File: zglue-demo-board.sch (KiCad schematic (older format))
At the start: 146 parts, among them J1 3220-10-0100-00, J10 0473460001, J2 DF13A-2P-1.25H, J3 3220-10-0100-00, J4 2x20_Header_Female, J5 0473460001, J6 556500488, J7 556500488, J8 WE_686115148922, J9 WE_686115148922_FLIPPED, U1 MCP1700T-3302E_TT, U2 NTS0104BQ, U3 NTS0104BQ, U4 NTS0104BQ, U5 93LC56CT-IMC, U6 FT4232HQ, U7 NTB0104BQ, U8 NTB0104BQ, Y1 ASFLMB-12.000MHZ-LC-T

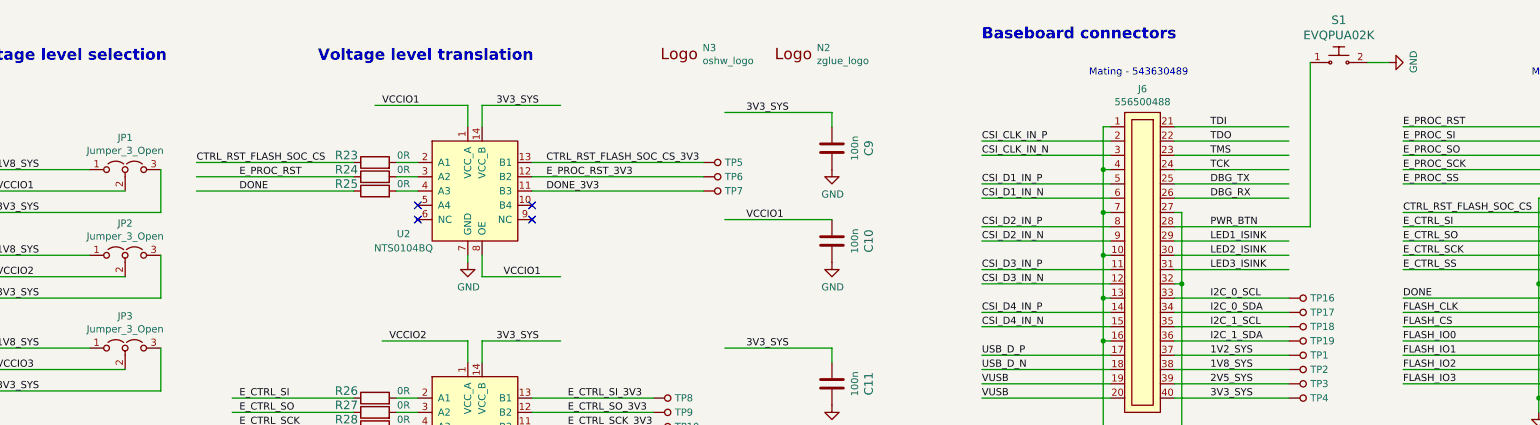
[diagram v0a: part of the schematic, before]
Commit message: Connected PWR_BTN to VUSB, updated PCB
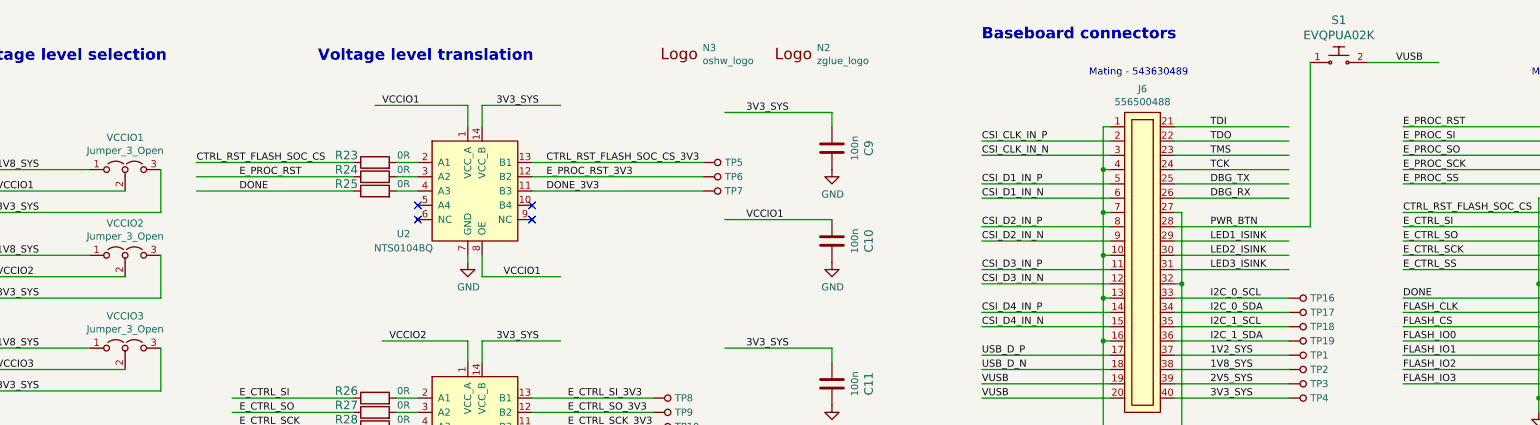
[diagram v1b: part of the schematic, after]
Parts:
- renumbered JP1 to VCCIO1, JP2 to VCCIO2, JP3 to VCCIO3
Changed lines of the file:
@@
 $EndComp
 $Comp
-L zglue-demo-board-rescue:Jumper_3_Open-Jumper JP2
+L zglue-demo-board-rescue:Jumper_3_Open-Jumper VCCIO2
 U 1 1 5F6F7935
 P 4350 2200
-F 0 "JP2" H 4350 2424 50  0000 C CNN
+F 0 "VCCIO2" H 4350 2424 50  0000 C CNN
 F 1 "Jumper_3_Open" H 4350 2333 50  0000 C CNN
 F 2 "Jumper:SolderJumper-3_P1.3mm_Open_Pad1.0x1.5mm" H 4350 2200 50  0001 C CNN
@@
 	4600 2500 3350 2500
 $Comp
-L zglue-demo-board-rescue:Jumper_3_Open-Jumper JP3
+L zglue-demo-board-rescue:Jumper_3_Open-Jumper VCCIO3
 U 1 1 5FF28200
 P 4350 2850
-F 0 "JP3" H 4350 3074 50  0000 C CNN
+F 0 "VCCIO3" H 4350 3074 50  0000 C CNN
 F 1 "Jumper_3_Open" H 4350 2983 50  0000 C CNN
 F 2 "Jumper:SolderJumper-3_P1.3mm_Open_Pad1.0x1.5mm" H 4350 2850 50  0001 C CNN
@@
 	4600 3150 3350 3150
 $Comp
-L zglue-demo-board-rescue:Jumper_3_Open-Jumper JP1
+L zglue-demo-board-rescue:Jumper_3_Open-Jumper VCCIO1
 U 1 1 5FF6DF38
 P 4350 1600
-F 0 "JP1" H 4350 1824 50  0000 C CNN
+F 0 "VCCIO1" H 4350 1824 50  0000 C CNN
 F 1 "Jumper_3_Open" H 4350 1733 50  0000 C CNN
 F 2 "Jumper:SolderJumper-3_P1.3mm_Open_Pad1.0x1.5mm" H 4350 1600 50  0001 C CNN
@@
 Wire Wire Line
 	11700 2000 12650 2000
-$Comp
-L power:GND #PWR0103
-U 1 1 5DCDFECB
-P 13200 850
-F 0 "#PWR0103" H 13200 600 50  0001 C CNN
-F 1 "GND" H 13205 677 50  0000 C CNN
-F 2 "" H 13200 850 50  0001 C CNN
-F 3 "" H 13200 850 50  0001 C CNN
-	1    13200 850
-	0    -1   -1   0
-$EndComp
-Wire Wire Line
-	13200 850  13050 850
+Wire Wire Line
+	13550 850  13050 850
 $Comp
 L antmicroLEDIndicationDiscrete:LG_L29K-G2J1-24-Z D9
@@
 	1    0    0    -1
 $EndComp
+Text Label 13250 850  0    50   ~ 0
+VUSB
 $EndSCHEMATC

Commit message: Layout components moved away from PCB edges
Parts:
- C1, C2, C3, C4, C5: footprint antmicro-footprints:0603-cap -> zglue-demo-board-footprints:0603-cap; symbol antmicroCapacitors0603:C_1u_0603 -> zglue-demo-board:C_1u_0603
- C10, C11, C12, C13, C14, C15, C16, C17, C18, C19, C20, C21, C22, C23, C24, C9: footprint antmicro-footprints:0402-cap -> zglue-demo-board-footprints:0402-cap; symbol antmicroCapacitors0402:C_100n_0402_6V3 -> zglue-demo-board:C_100n_0402_6V3
- C25, C26: footprint antmicro-footprints:0402-cap -> zglue-demo-board-footprints:0402-cap; symbol antmicroCapacitors0402:C_4u7_0402 -> zglue-demo-board:C_4u7_0402
- D1, D3, D4: footprint antmicro-footprints:SOD-123 -> zglue-demo-board-footprints:SOD-123; symbol antmicroDiodesRectifiersSingle:MBR0540T1G -> zglue-demo-board:MBR0540T1G
- D10, D11, D12, D13, D6, D7, D8, D9: footprint antmicro-footprints:LED_0603 -> zglue-demo-board-footprints:LED_0603; symbol antmicroLEDIndicationDiscrete:LG_L29K-G2J1-24-Z -> zglue-demo-board:LG_L29K-G2J1-24-Z
- D2, D5: footprint antmicro-footprints:SOT-3 -> zglue-demo-board-footprints:SOT-3; symbol antmicroTVSDiodes:TPD2EUSB30DRTR -> zglue-demo-board:TPD2EUSB30DRTR
- FB1, FB2: footprint antmicro-footprints:0603-res -> zglue-demo-board-footprints:0603; symbol antmicroFerriteBeadsandChips:BLM18AG601SN1D -> zglue-demo-board:BLM18AG601SN1D
- J1, J3: footprint antmicro-footprints:PinHeader_2x5_P1.27mm_Drill.7mm -> zglue-demo-board-footprints:PinHeader_2x5_P1.27mm_Drill.7mm; symbol antmicroRectangularConnectorsHeadersMalePins:3220-10-0100-00 -> zglue-demo-board:3220-10-0100-00
- J10, J5: footprint antmicro-footprints:USB_Micro_B_Female_0473460001 -> zglue-demo-board-footprints:USB_Micro_B_Female_0473460001; symbol antmicroUSBDVIHDMIConnectors:0473460001 -> zglue-demo-board:0473460001
- J2: footprint antmicro-footprints:DF13A-2P-1.25H -> zglue-demo-board-footprints:DF13A-2P-1.25H; symbol antmicroDF13Connectors:DF13A-2P-1.25H -> zglue-demo-board:DF13A-2P-1.25H
- J4: footprint antmicro-footprints:PinHeader_2x40_P2.54_Drill1mm -> zglue-demo-board-footprints:PinHeader_2x40_P2.54_Drill1mm; symbol antmicroRectangularConnectorsHeadersFemalePins:2x20_Header_Female -> zglue-demo-board:2x20_Header_Female
- J6, J7: footprint antmicro-footprints:556500488 -> zglue-demo-board-footprints:556500488; symbol antmicroB2bConnectors:556500488 -> zglue-demo-board:556500488; MPN (none) -> 556500488; Manufacturer (none) -> Molex
- J8: footprint antmicro-footprints:WE_686115148922 -> zglue-demo-board-footprints:WE_686115148922; symbol antmicroFCCConnectors:WE_686115148922 -> zglue-demo-board:WE_686115148922
- J9: footprint antmicro-footprints:WE_686115148922_FLIPPED -> zglue-demo-board-footprints:WE_686115148922_FLIPPED; symbol antmicroFCCConnectors:WE_686115148922_FLIPPED -> zglue-demo-board:WE_686115148922_FLIPPED
- N1: footprint antmicro-footprints:antmicro-logo_scaled_20mm -> zglue-demo-board-footprints:antmicro-logo; symbol antmicroMechanicalParts:antmicro_logo -> zglue-demo-board:antmicro_logo
- N2: footprint antmicro-footprints:zglue-logo -> zglue-demo-board-footprints:zglue-logo; symbol antmicroMechanicalParts:zglue_logo -> zglue-demo-board:zglue_logo
- N3: footprint antmicro-footprints:oshw-logo -> zglue-demo-board-footprints:oshw-logo; symbol antmicroMechanicalParts:oshw_logo -> zglue-demo-board:oshw_logo
- R1: footprint antmicro-footprints:0603-res -> zglue-demo-board-footprints:0603-res; symbol antmicroResistors0603:R_0R_0603 -> zglue-demo-board:R_0R_0603
- R10, R5: footprint antmicro-footprints:0402-res -> zglue-demo-board-footprints:0402-res; symbol antmicroResistors0402:R_2k_0402 -> zglue-demo-board:R_2k_0402
- R11, R12, R13, R14, R15, R16, R17, R18, R19, R2, R20, R21, R22, R23, R24, R25, R26, R27, R28, R29, R3, R30, R31, R32, R33, R42, R43, R44, R45, R46, R47, R48, R49, R50, R51, R52, R53, R54, R55, R56, R57, R58, R59, R8: footprint antmicro-footprints:0402-res -> zglue-demo-board-footprints:0402-res; symbol antmicroResistors0402:R_0R_0402 -> zglue-demo-board:R_0R_0402
- R34: footprint antmicro-footprints:0402-res -> zglue-demo-board-footprints:0402-res; symbol antmicroResistors0402:R_470R_0402 -> zglue-demo-board:R_470R_0402
- R35, R36, R37, R38, R39, R40, R41: footprint antmicro-footprints:0402-res -> zglue-demo-board-footprints:0402-res; symbol antmicroResistors0402:R_330R_0402 -> zglue-demo-board:R_330R_0402
- R4, R6, R7: footprint antmicro-footprints:0402-res -> zglue-demo-board-footprints:0402-res; symbol antmicroResistors0402:R_10k_0402 -> zglue-demo-board:R_10k_0402
- R9: footprint antmicro-footprints:0402-res -> zglue-demo-board-footprints:0402-res; symbol antmicroResistors0402:R_12k_0402 -> zglue-demo-board:R_12k_0402
- S1: footprint antmicro-footprints:Panasonic_EVQPUJ_EVQPUA -> zglue-demo-board-footprints:Panasonic_EVQPUJ_EVQPUA; symbol antmicroTactileSwitches:EVQPUA02K -> zglue-demo-board:EVQPUA02K
- TP1, TP10, TP11, TP12, TP13, TP14, TP15, TP16, TP17, TP18, TP19, TP2, TP20, TP21, TP22, TP23, TP3, TP4, TP5, TP6, TP7, TP8, TP9: footprint antmicro-footprints:Testpoint_smd_1mm -> zglue-demo-board-footprints:Testpoint_smd_1mm; symbol antmicroTestPoints:TP_SMD1MM -> zglue-demo-board:TP_SMD1MM
- U1: footprint antmicro-footprints:SOT-23-3 -> zglue-demo-board-footprints:SOT-23-3; symbol antmicroPMICVoltageRegulatorsLinear:MCP1700T-3302E_TT -> zglue-demo-board:MCP1700T-3302E_TT
- U2, U3, U4: footprint antmicro-footprints:QDHVQFN14 -> zglue-demo-board-footprints:QDHVQFN14; symbol antmicroLogicTranslatorsLevelShifters:NTS0104BQ -> zglue-demo-board:NTS0104BQ
- U5: footprint antmicro-footprints:DFN-8_2x3mm -> zglue-demo-board-footprints:DFN-8_2x3mm; symbol antmicroMemory:93LC56CT-IMC -> zglue-demo-board:93LC56CT-IMC
- U6: footprint antmicro-footprints:FT4232HQ -> zglue-demo-board-footprints:FT4232HQ; symbol antmicroInterfaceControllers:FT4232HQ -> zglue-demo-board:FT4232HQ
- U7, U8: footprint antmicro-footprints:QDHVQFN14 -> zglue-demo-board-footprints:QDHVQFN14; symbol antmicroLogicTranslatorsLevelShifters:NTB0104BQ -> zglue-demo-board:NTB0104BQ
- VCCIO1, VCCIO2, VCCIO3: symbol zglue-demo-board-rescue:Jumper_3_Open-Jumper -> zglue-demo-board:Jumper_3_Open-Jumper
- Y1: footprint antmicro-footprints:ASFLMB -> zglue-demo-board-footprints:ASFLMB; symbol antmicroOscillators:ASFLMB-12.000MHZ-LC-T -> zglue-demo-board:ASFLMB-12.000MHZ-LC-T
